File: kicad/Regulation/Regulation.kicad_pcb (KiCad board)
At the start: 2 copper layers, 98 x 50 mm, 48 parts, among them J1 Screw_Terminal_01x02, J2 Conn_02x05_Odd_Even, J3 Screw_Terminal_01x02, K1 G6A, Q1 2N3904, Q2 2N3904, Q3 2N3904, Q4 TIP32C, Q5 2N3904, U1 LM7805_TO220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

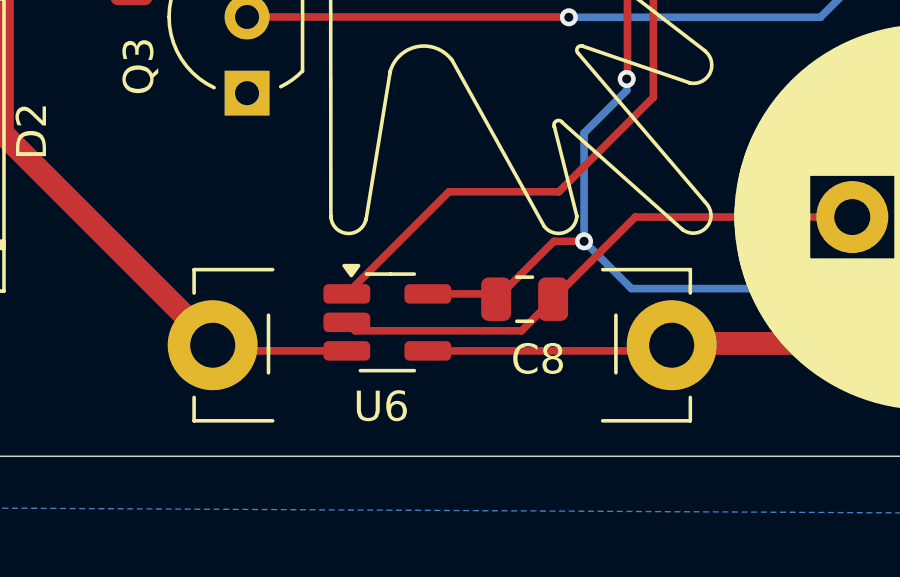
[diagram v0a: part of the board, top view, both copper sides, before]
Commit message: Fix control connectors spacing
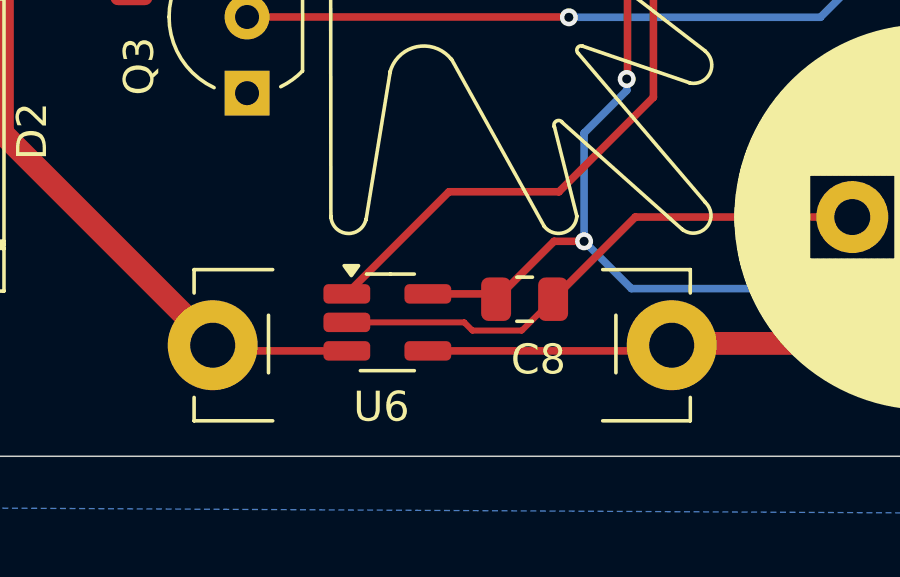
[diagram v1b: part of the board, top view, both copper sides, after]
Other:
- rule pad_to_mask_clearance: 0.0508 -> 0
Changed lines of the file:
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@@
 			(dielectric_constraints no)
 		)
-		(pad_to_mask_clearance 0.0508)
+		(pad_to_mask_clearance 0)
 		(allow_soldermask_bridges_in_footprints no)
 		(pcbplotparams
-			(layerselection 0x00010fc_ffffffff)
+			(layerselection 0x00010f0_ffffffff)
 			(plot_on_all_layers_selection 0x0000000_00000000)
 			(disableapertmacros no)
@@
 	)
 	(segment
-		(start 175.768 117.468)
-		(end 174.8 116.5)
-		(width 0.254)
+		(start 130.067 148.037)
+		(end 130.34 148.31)
+		(width 0.2)
 		(layer "F.Cu")
 		(net 1)
 	)
 	(segment
-		(start 126.434 148.3168)
-		(end 131.978 148.3168)
+		(start 175.768 117.468)
+		(end 174.8 116.5)
 		(width 0.254)
 		(layer "F.Cu")
@@
 	)
 	(segment
+		(start 130.34 148.31)
+		(end 131.9848 148.31)
+		(width 0.2)
+		(layer "F.Cu")
+		(net 1)
+	)
+	(segment
 		(start 166.243 105.918)
 		(end 165.782 105.918)
@@
 	)
 	(segment
-		(start 126.1542 148.037)
-		(end 126.434 148.3168)
-		(width 0.254)
-		(layer "F.Cu")
-		(net 1)
-	)
-	(segment
 		(start 165.782 105.918)
 		(end 162.88 108.82)
@@
 	)
 	(segment
+		(start 126.1542 148.037)
+		(end 130.067 148.037)
+		(width 0.2)
+		(layer "F.Cu")
+		(net 1)
+	)
+	(segment
+		(start 131.9848 148.31)
+		(end 133.03 147.2648)
+		(width 0.2)
+		(layer "F.Cu")
+		(net 1)
+	)
+	(segment
 		(start 135.7688 144.526)
 		(end 143.002 144.526)
@@
 		(layer "F.Cu")
 		(net 1)
-	)
-	(segment
-		(start 131.978 148.3168)
-		(end 133.03 147.2648)
-		(width 0.254)
-		(layer "F.Cu")
-		(net 1)
